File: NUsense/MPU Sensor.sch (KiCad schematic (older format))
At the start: 4 parts, among them U9? MPU6000

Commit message: Change hierarchy layout
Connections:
- net MPU_SDA/SDI renamed MPU_SDA?SDI
- net VDD5o5V renamed +3V3
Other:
- moved on the sheet: 2.2nF
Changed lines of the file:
@@
 LIBS:valves
 LIBS:ADM6713RAKS
+LIBS:Header_Connectors
 LIBS:MPU6000
 LIBS:NUbots
 LIBS:STM32F746ZGT6
-LIBS:Header_Connectors
 LIBS:NUsense-cache
 EELAYER 25 0
@@
 L GND #PWR?
 U 1 1 5A698AEC
-P 4650 3800
-F 0 "#PWR?" H 4650 3550 50  0001 C CNN
-F 1 "GND" H 4650 3650 50  0000 C CNN
-F 2 "" H 4650 3800 50  0001 C CNN
-F 3 "" H 4650 3800 50  0001 C CNN
-	1    4650 3800
+P 4600 3800
+F 0 "#PWR?" H 4600 3550 50  0001 C CNN
+F 1 "GND" H 4600 3650 50  0000 C CNN
+F 2 "" H 4600 3800 50  0001 C CNN
+F 3 "" H 4600 3800 50  0001 C CNN
+	1    4600 3800
 	1    0    0    -1
 $EndComp
@@
 Wire Wire Line
 	6250 2850 6850 2850
-Text GLabel 6750 2100 1    60   Input ~ 0
-VDD5o5V
 $Comp
 L C 0.1uF
@@
 L C 2.2nF
 U 1 1 5A6D2BCA
-P 4650 3400
-F 0 "2.2nF" H 4675 3500 50  0000 L CNN
-F 1 "C" H 4675 3300 50  0000 L CNN
-F 2 "" H 4688 3250 50  0001 C CNN
-F 3 "" H 4650 3400 50  0001 C CNN
-	1    4650 3400
+P 4600 3400
+F 0 "2.2nF" H 4625 3500 50  0000 L CNN
+F 1 "C" H 4625 3300 50  0000 L CNN
+F 2 "" H 4638 3250 50  0001 C CNN
+F 3 "" H 4600 3400 50  0001 C CNN
+	1    4600 3400
 	1    0    0    -1
 $EndComp
 Wire Wire Line
-	5000 2450 4650 2450
-Wire Wire Line
-	4200 2850 5000 2850
-Wire Wire Line
-	4200 2750 5000 2750
+	4600 2450 5000 2450
 Wire Wire Line
 	6250 3250 7750 3250
@@
 Wire Wire Line
 	7150 3350 7150 3500
-Text GLabel 7750 3250 2    60   Input ~ 0
-MPU_INT
-Text GLabel 4200 2850 0    60   Input ~ 0
-MPU_SDA/SDI
-Text GLabel 4200 2750 0    60   Input ~ 0
-MPU_SCL
 Wire Wire Line
 	5000 3250 4850 3250
@@
 	4850 3250 4850 3650
 Wire Wire Line
-	4850 3650 4650 3650
+	4850 3650 4600 3650
 Wire Wire Line
-	4650 3550 4650 3800
-Connection ~ 4650 3650
+	4600 3550 4600 3800
+Connection ~ 4600 3650
 Wire Wire Line
-	4650 2450 4650 3250
+	4600 2450 4600 3250
+$Comp
+L +3.3V #PWR?
+U 1 1 5A6FD48D
+P 6750 2100
+F 0 "#PWR?" H 6750 1950 50  0001 C CNN
+F 1 "+3.3V" H 6750 2240 50  0000 C CNN
+F 2 "" H 6750 2100 50  0001 C CNN
+F 3 "" H 6750 2100 50  0001 C CNN
+	1    6750 2100
+	1    0    0    -1
+$EndComp
+Wire Wire Line
+	4200 2850 5000 2850
+Wire Wire Line
+	5000 2750 4200 2750
+Text HLabel 4200 2750 0    60   Output ~ 0
+MPU_SCL
+Text HLabel 4200 2850 0    60   Output ~ 0
+MPU_SDA?SDI
+Text HLabel 7750 3250 2    60   Output ~ 0
+MPU_INT
 $EndSCHEMATC

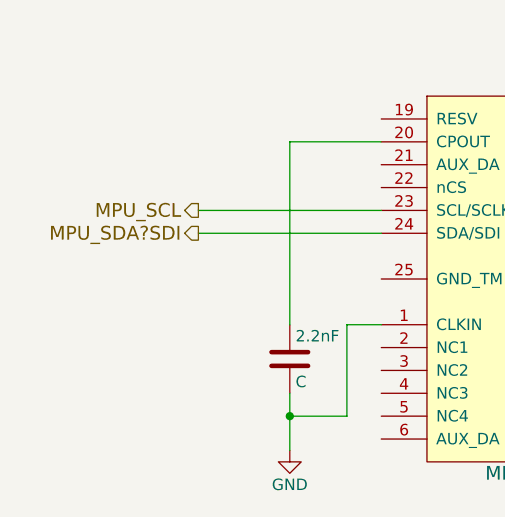
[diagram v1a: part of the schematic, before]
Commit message: Add power components
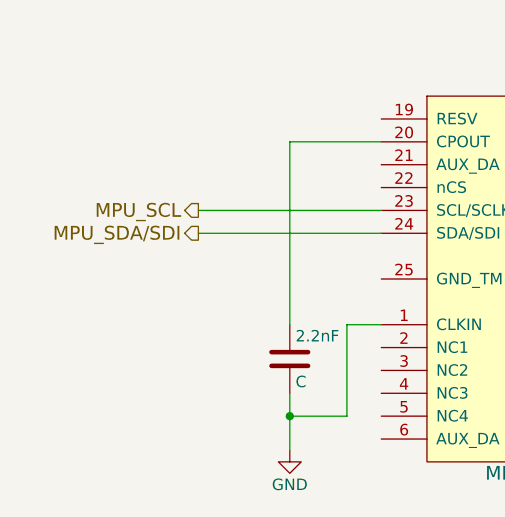
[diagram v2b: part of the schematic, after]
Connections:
- net MPU_SDA?SDI renamed MPU_SDA/SDI
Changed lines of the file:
@@
 MPU_SCL
 Text HLabel 4200 2850 0    60   Output ~ 0
-MPU_SDA?SDI
+MPU_SDA/SDI
 Text HLabel 7750 3250 2    60   Output ~ 0
 MPU_INT

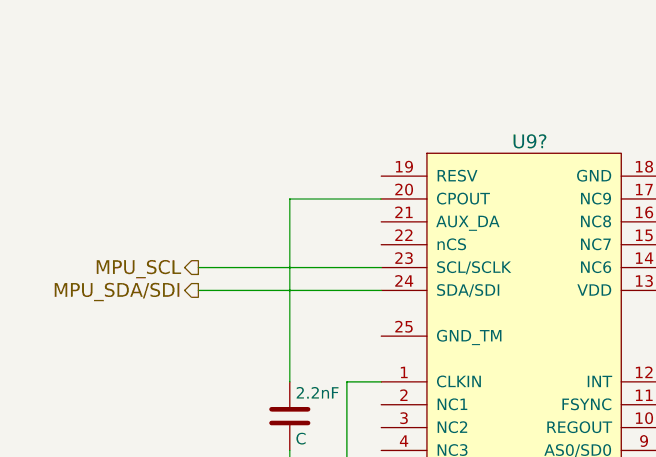
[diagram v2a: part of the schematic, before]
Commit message: Update Component Values
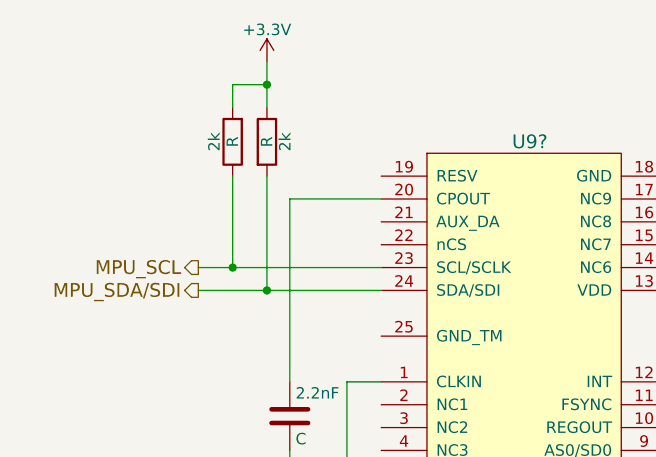
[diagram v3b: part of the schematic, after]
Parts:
- added 2k (x2): R, symbol R
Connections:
- net +3V3: now also 2k.1, 2k.2
- net MPU_SCL: now also 2k.1
- net MPU_SDA/SDI: now also 2k.2
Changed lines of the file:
@@
 Text HLabel 7750 3250 2    60   Output ~ 0
 MPU_INT
+$Comp
+L R 2k
+U 1 1 5A70093B
+P 4500 2200
+F 0 "2k" V 4580 2200 50  0000 C CNN
+F 1 "R" V 4500 2200 50  0000 C CNN
+F 2 "" V 4430 2200 50  0001 C CNN
+F 3 "" H 4500 2200 50  0001 C CNN
+	1    4500 2200
+	1    0    0    -1
+$EndComp
+$Comp
+L R 2k
+U 1 1 5A700977
+P 4350 2200
+F 0 "2k" V 4430 2200 50  0000 C CNN
+F 1 "R" V 4350 2200 50  0000 C CNN
+F 2 "" V 4280 2200 50  0001 C CNN
+F 3 "" H 4350 2200 50  0001 C CNN
+	1    4350 2200
+	-1   0    0    1
+$EndComp
+Wire Wire Line
+	4350 2350 4350 2750
+Connection ~ 4350 2750
+Wire Wire Line
+	4500 2350 4500 2850
+Connection ~ 4500 2850
+Wire Wire Line
+	4500 1850 4500 2050
+Wire Wire Line
+	4500 1950 4350 1950
+Wire Wire Line
+	4350 1950 4350 2050
+Connection ~ 4500 1950
+$Comp
+L +3.3V #PWR?
+U 1 1 5A700A52
+P 4500 1850
+F 0 "#PWR?" H 4500 1700 50  0001 C CNN
+F 1 "+3.3V" H 4500 1990 50  0000 C CNN
+F 2 "" H 4500 1850 50  0001 C CNN
+F 3 "" H 4500 1850 50  0001 C CNN
+	1    4500 1850
+	1    0    0    -1
+$EndComp
 $EndSCHEMATC

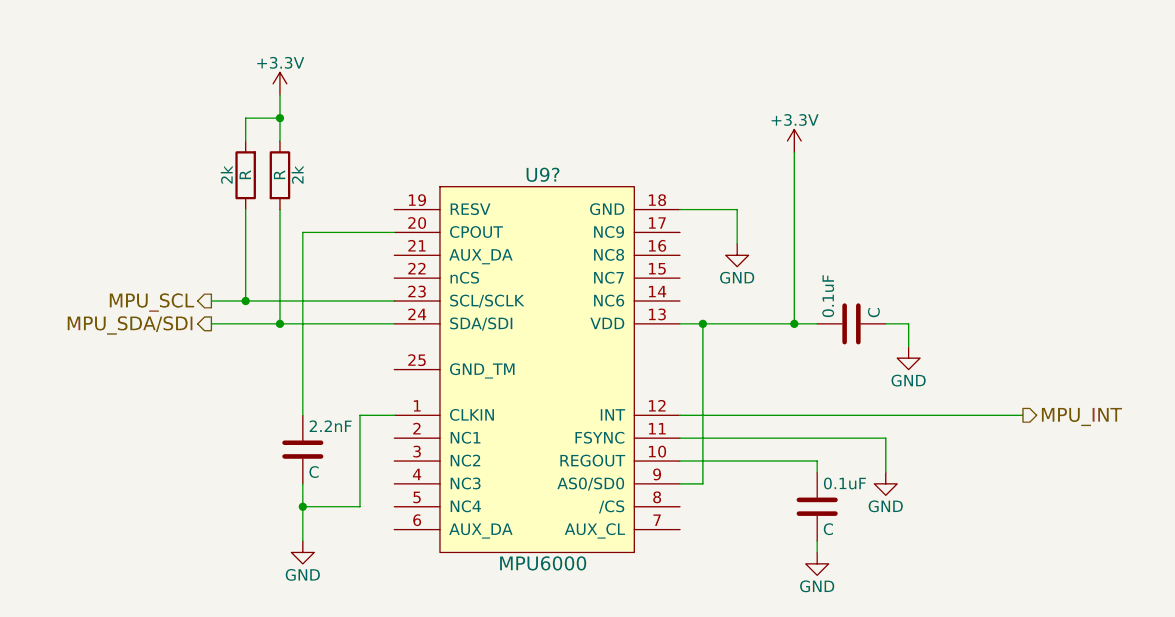
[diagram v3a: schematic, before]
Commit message: Update component values
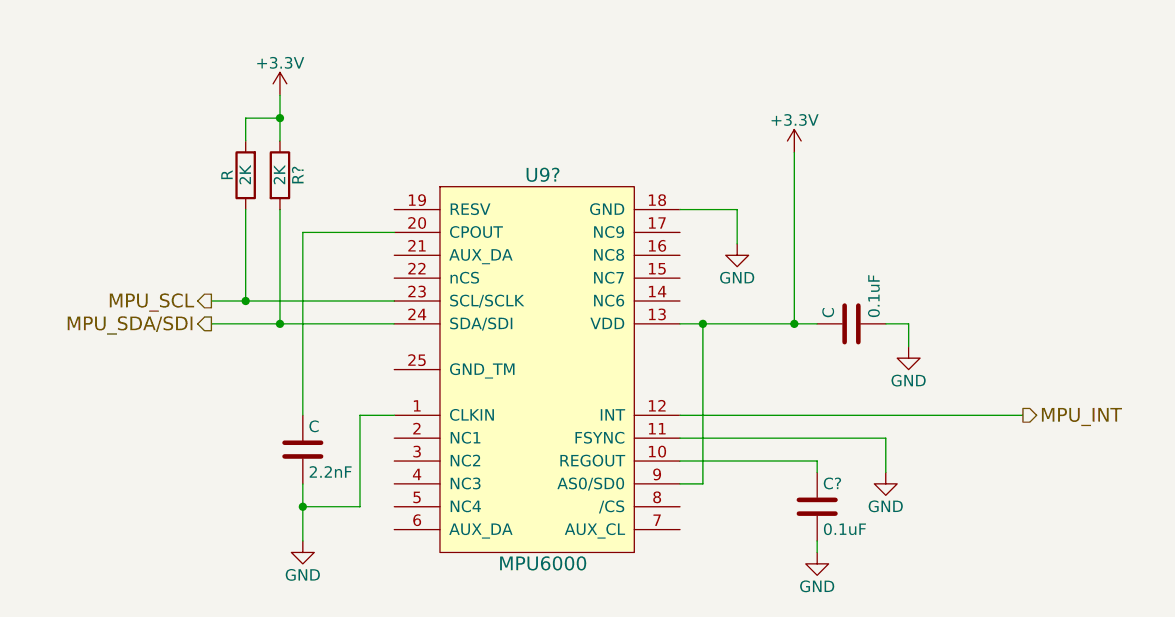
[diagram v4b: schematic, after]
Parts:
- removed 0.1uF: C, symbol C
- removed 2k: R, symbol R
- added C?: 0.1uF, symbol C
- added R?: 2K, symbol R
- C: renamed from 0.1uF; value C -> 0.1uF
- C: renamed from 2.2nF; value C -> 2.2nF
- R: renamed from 2k; value R -> 2K
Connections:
- net +3V3: now also R?.1
- net GND: now also C?.2
- net MPU_SDA/SDI: now also R?.2
- net at U9?.10 (REGOUT): now also C?.1
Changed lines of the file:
@@
 	6250 2850 6850 2850
 $Comp
-L C 0.1uF
+L C C
 U 1 1 5A6D29D1
 P 7000 2850
-F 0 "0.1uF" H 7025 2950 50  0000 L CNN
-F 1 "C" H 7025 2750 50  0000 L CNN
+F 0 "C" H 7025 2950 50  0000 L CNN
+F 1 "0.1uF" H 7025 2750 50  0000 L CNN
 F 2 "" H 7038 2700 50  0001 C CNN
 F 3 "" H 7000 2850 50  0001 C CNN
@@
 	1    0    0    -1
 $EndComp
-$Comp
-L C 0.1uF
-U 1 1 5A6D2B51
-P 6850 3650
-F 0 "0.1uF" H 6875 3750 50  0000 L CNN
-F 1 "C" H 6875 3550 50  0000 L CNN
-F 2 "" H 6888 3500 50  0001 C CNN
-F 3 "" H 6850 3650 50  0001 C CNN
-	1    6850 3650
-	1    0    0    -1
-$EndComp
 Wire Wire Line
 	6850 3450 6850 3500
@@
 	6850 3800 6850 3850
 $Comp
-L C 2.2nF
+L C C
 U 1 1 5A6D2BCA
 P 4600 3400
-F 0 "2.2nF" H 4625 3500 50  0000 L CNN
-F 1 "C" H 4625 3300 50  0000 L CNN
+F 0 "C" H 4625 3500 50  0000 L CNN
+F 1 "2.2nF" H 4625 3300 50  0000 L CNN
 F 2 "" H 4638 3250 50  0001 C CNN
 F 3 "" H 4600 3400 50  0001 C CNN
@@
 MPU_INT
 $Comp
-L R 2k
-U 1 1 5A70093B
-P 4500 2200
-F 0 "2k" V 4580 2200 50  0000 C CNN
-F 1 "R" V 4500 2200 50  0000 C CNN
-F 2 "" V 4430 2200 50  0001 C CNN
-F 3 "" H 4500 2200 50  0001 C CNN
-	1    4500 2200
-	1    0    0    -1
-$EndComp
-$Comp
-L R 2k
+L R R
 U 1 1 5A700977
 P 4350 2200
-F 0 "2k" V 4430 2200 50  0000 C CNN
-F 1 "R" V 4350 2200 50  0000 C CNN
+F 0 "R" V 4430 2200 50  0000 C CNN
+F 1 "2K" V 4350 2200 50  0000 C CNN
 F 2 "" V 4280 2200 50  0001 C CNN
 F 3 "" H 4350 2200 50  0001 C CNN
@@
 	1    0    0    -1
 $EndComp
+$Comp
+L R R?
+U 1 1 5A704E41
+P 4500 2200
+F 0 "R?" V 4580 2200 50  0000 C CNN
+F 1 "2K" V 4500 2200 50  0000 C CNN
+F 2 "" V 4430 2200 50  0001 C CNN
+F 3 "" H 4500 2200 50  0001 C CNN
+	1    4500 2200
+	1    0    0    -1
+$EndComp
+$Comp
+L C C?
+U 1 1 5A704EA0
+P 6850 3650
+F 0 "C?" H 6875 3750 50  0000 L CNN
+F 1 "0.1uF" H 6875 3550 50  0000 L CNN
+F 2 "" H 6888 3500 50  0001 C CNN
+F 3 "" H 6850 3650 50  0001 C CNN
+	1    6850 3650
+	1    0    0    -1
+$EndComp
